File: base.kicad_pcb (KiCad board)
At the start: 2 copper layers, 100 x 100 mm, 110 parts, among them J1 Screw_Terminal_01x02, J2 Out, Q2 MJD31C, Q3 IPD50R3K0CE, Q4 MJD31C, Q5 MMBTA42, Q6 MMBTA42, Q7 MMBTA42, Q8 MMBTA42, T1 FL2015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

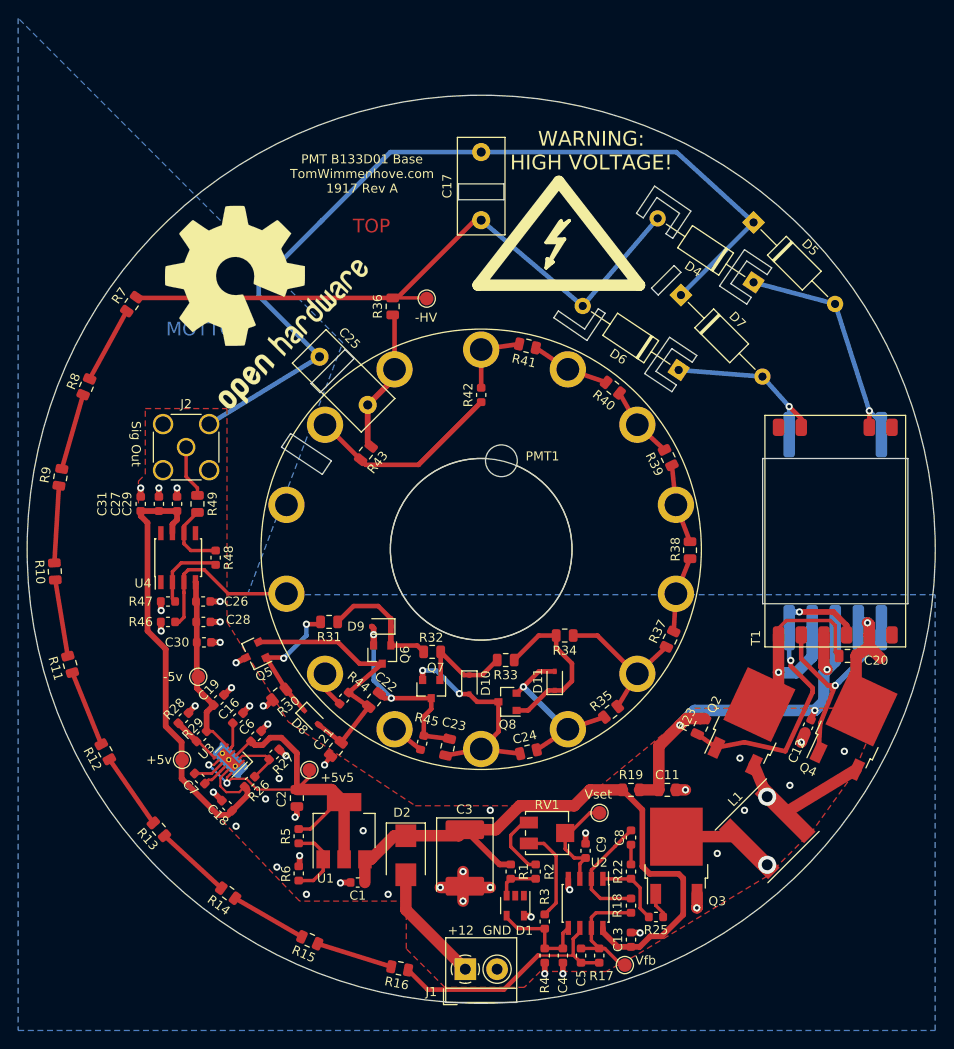
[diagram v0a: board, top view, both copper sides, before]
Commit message: Changed royer circuit cap to TH
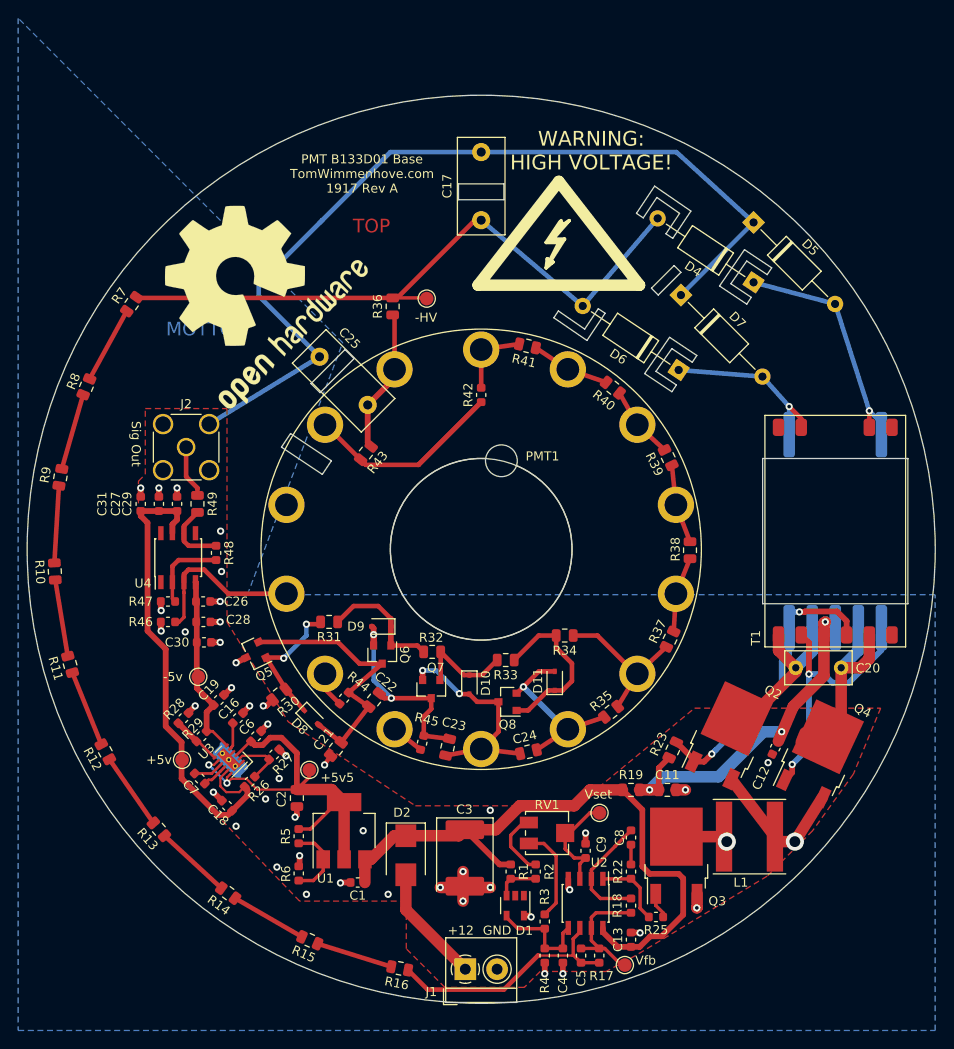
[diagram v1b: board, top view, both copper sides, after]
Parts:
- C20: value 220n -> 47n; footprint Capacitor_SMD:C_0805_2012Metric -> Capacitor_THT:C_Rect_L7.2mm_W3.5mm_P5.00mm_FKS2_FKP2_MKS2_MKP2
- moved C20 5.85 mm to (134.7, 113.0)
- moved Q4 4.80 mm to (137.3, 122.5)
- moved C12 4.30 mm to (132.4, 121.8)
- moved R23 4.05 mm to (121.1, 122.1), turned to 65 degrees
- moved Q2 2.94 mm to (127.2, 120.5)
- moved L1 2.06 mm to (129.6, 131.7), turned to 180 degrees
- moved R48 0.53 mm to (70.8, 100.4)
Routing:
- net Net-(C20-Pad2): track 13.6 -> 25.0 mm, vias 1 -> 0
- net Net-(C20-Pad1): track 27.3 -> 18.7 mm, vias 1 -> 0
- net Net-(Q4-Pad1): track 24.3 -> 29.5 mm, vias 1 -> 2
- net Net-(C11-Pad1): track 43.9 -> 39.8 mm
- net Net-(L1-Pad2): track 8.57 -> 5.78 mm
- net Net-(Q2-Pad1): track 36.0 -> 33.4 mm
- net GND: track 156.1 -> 155.0 mm, vias 46 -> 43
- net (no net): vias 0 -> 1

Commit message: Fixed some footprints and values
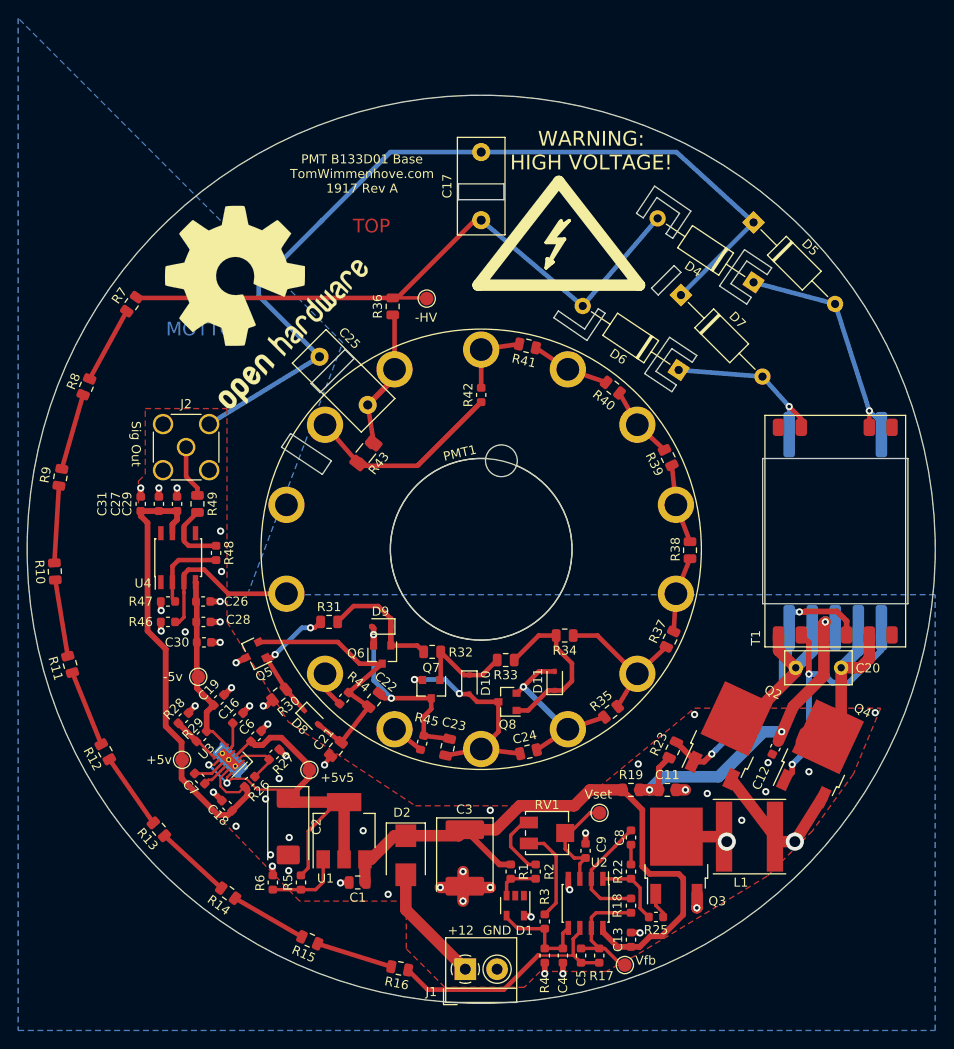
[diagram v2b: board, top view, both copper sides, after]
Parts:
- C1: footprint Capacitor_SMD:C_0603_1608Metric -> Capacitor_SMD:C_0805_2012Metric
- C2: value 100u -> 100u/16v; footprint Capacitor_SMD:C_0805_2012Metric -> Capacitor_Tantalum_SMD:CP_EIA-7343-30_AVX-N
- R23: value 820 -> 2k2
- R43: footprint Resistor_SMD:R_0805_2012Metric -> Resistor_SMD:R_1206_3216Metric
- moved R5 5.11 mm to (80.2, 136.7)
- moved C2 3.29 mm to (78.8, 130.6)
- moved R6 3.02 mm to (77.0, 136.7)
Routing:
- net Net-(C2-Pad1): track 47.8 -> 55.1 mm
- net GND: track 155.0 -> 153.6 mm, vias 43 -> 50
- net Net-(PMT1-Pad13): track 31.8 -> 32.9 mm
- net Net-(R5-Pad1): track 8.30 -> 9.20 mm
- net Net-(D8-Pad1): track 15.6 -> 14.8 mm

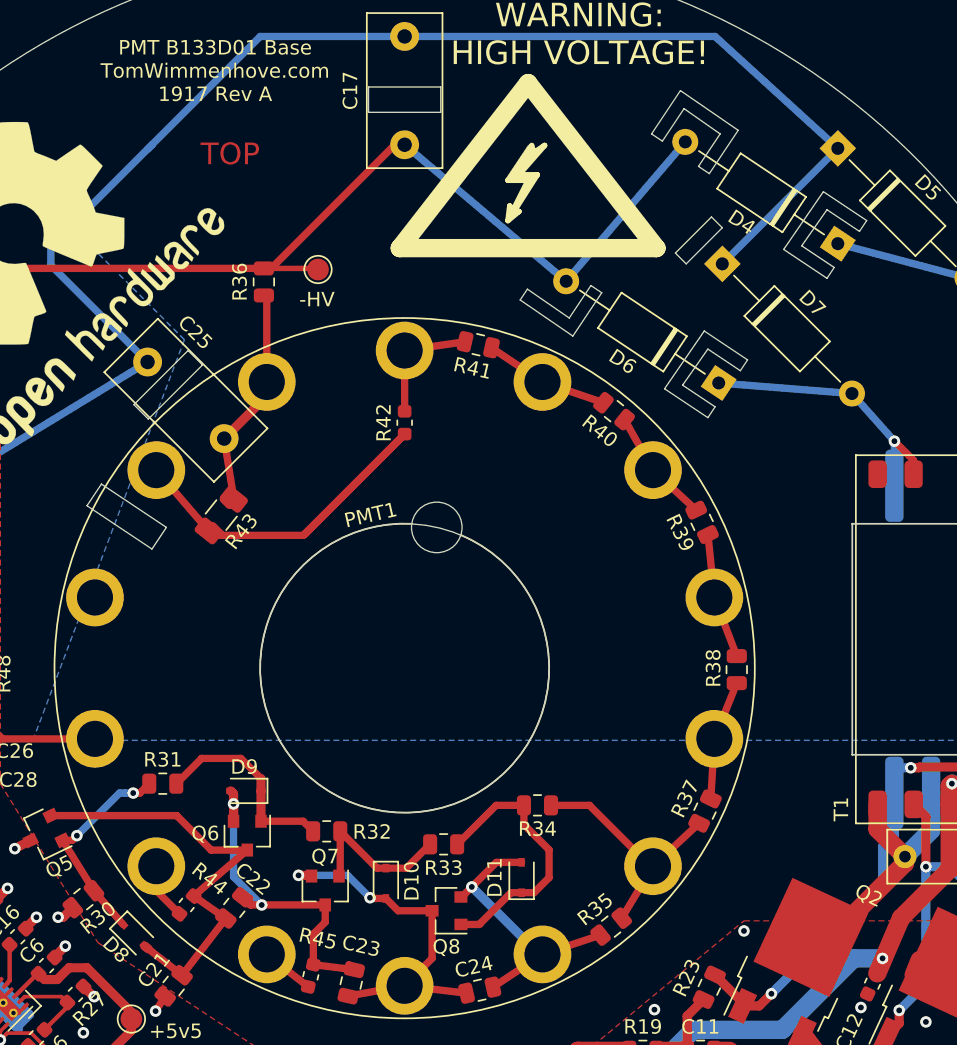
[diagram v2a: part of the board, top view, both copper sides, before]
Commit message: Added slots foot prints
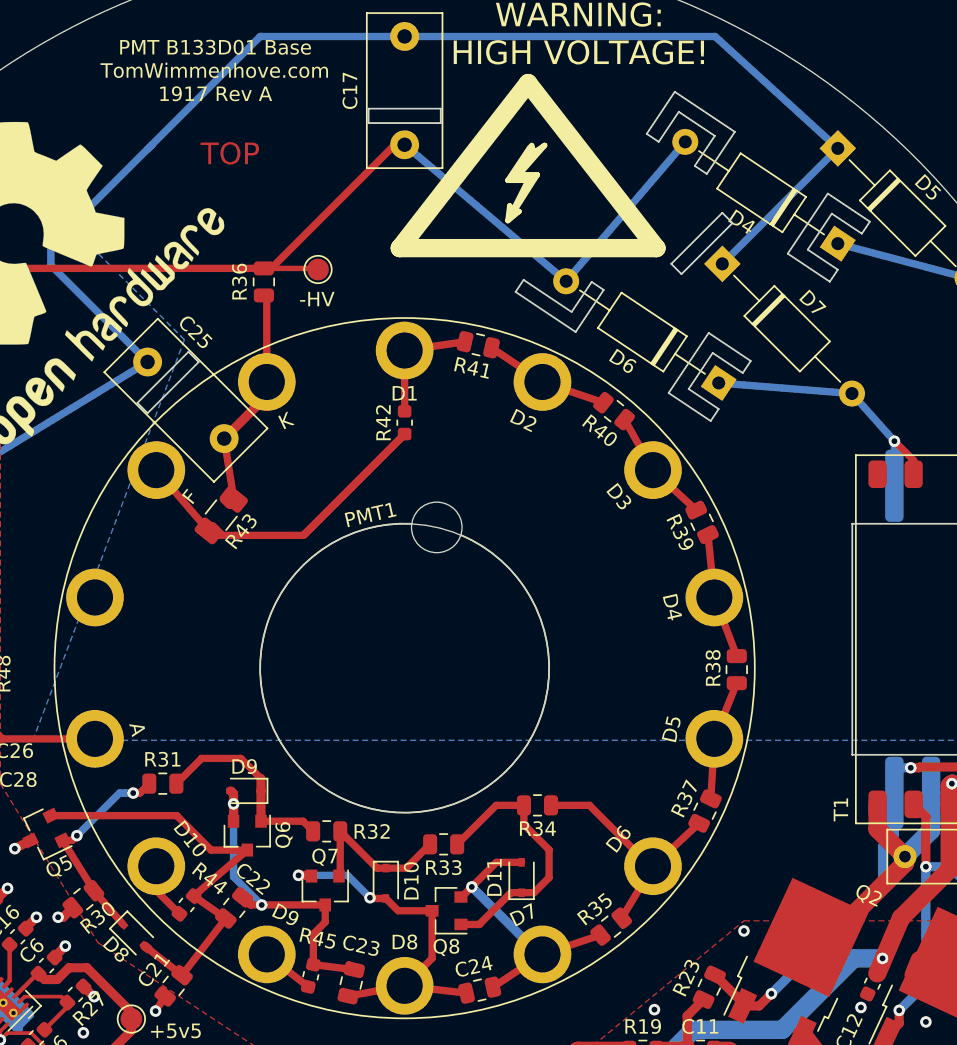
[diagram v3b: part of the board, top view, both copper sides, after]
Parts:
- added Slot**: ISlot, slots:ISlot, F.Cu at (82.2, 78.8)
- added Slot**: ISlot, slots:ISlot, F.Cu at (100.0, 63.8)
- added Slot**: CSlot, slots:CSlot, F.Cu at (121.8, 80.2)
- added Slot**: CSlot, slots:CSlot, F.Cu at (130.0, 70.6)
- added Slot**: LSlot, slots:LSlot, F.Cu at (111.2, 73.2)
- added Slot**: ISlot, slots:ISlot, F.Cu at (122.0, 72.0)
- added Slot**: CSlot, slots:CSlot, F.Cu at (119.4, 63.5)
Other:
- outline, holes or cut-outs redrawn

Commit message: Small fix
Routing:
- net GND: track 153.6 -> 154.6 mm
- net (no net): vias 1 -> 0

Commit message: Layout changes
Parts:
- moved R6 4.99 mm to (82.0, 136.7), turned to 90 degrees
- moved R5 4.18 mm to (84.3, 136.7), turned to 270 degrees
- moved R42 3.05 mm to (98.0, 85.3), turned to 45 degrees
- moved C1 0.51 mm to (86.9, 136.9), turned to 270 degrees
- moved U1 0.44 mm to (84.9, 130.6)
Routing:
- net Net-(PMT1-Pad13): track 32.9 -> 19.4 mm
- net Net-(C2-Pad1): track 55.1 -> 49.1 mm
- net Net-(PMT1-Pad1): track 8.44 -> 11.6 mm
- net Net-(R5-Pad1): track 9.20 -> 7.26 mm
- net GND: track 154.6 -> 154.7 mm, vias 50 -> 49
